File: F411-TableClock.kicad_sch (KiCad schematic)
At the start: 43 parts, among them J1 USB_C_Receptacle_USB2.0_16P, J2 Conn_01x16_Socket, J4 Conn_01x04_Pin, J5 Conn_01x08_Socket, J6 Conn_01x08_Pin, Q1 DMG3415U, Q2 BC547, SW1 SW_Push, SW2 SW_Push, SW3 SW_Push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

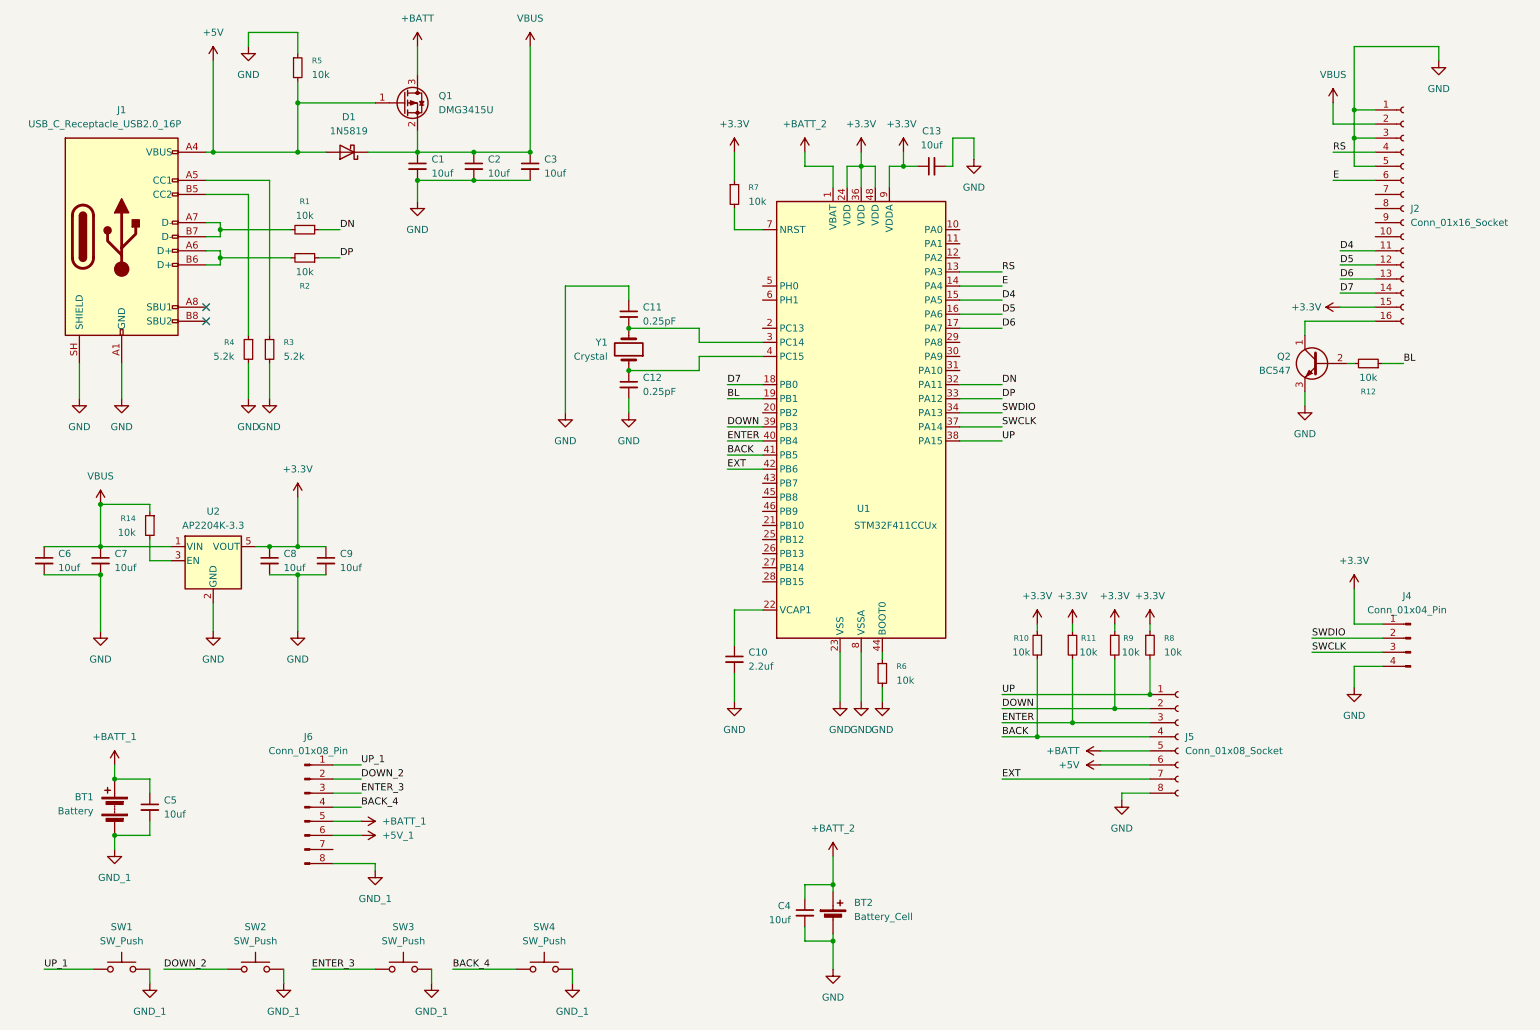
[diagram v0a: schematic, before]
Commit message: DHT added F411 table clock
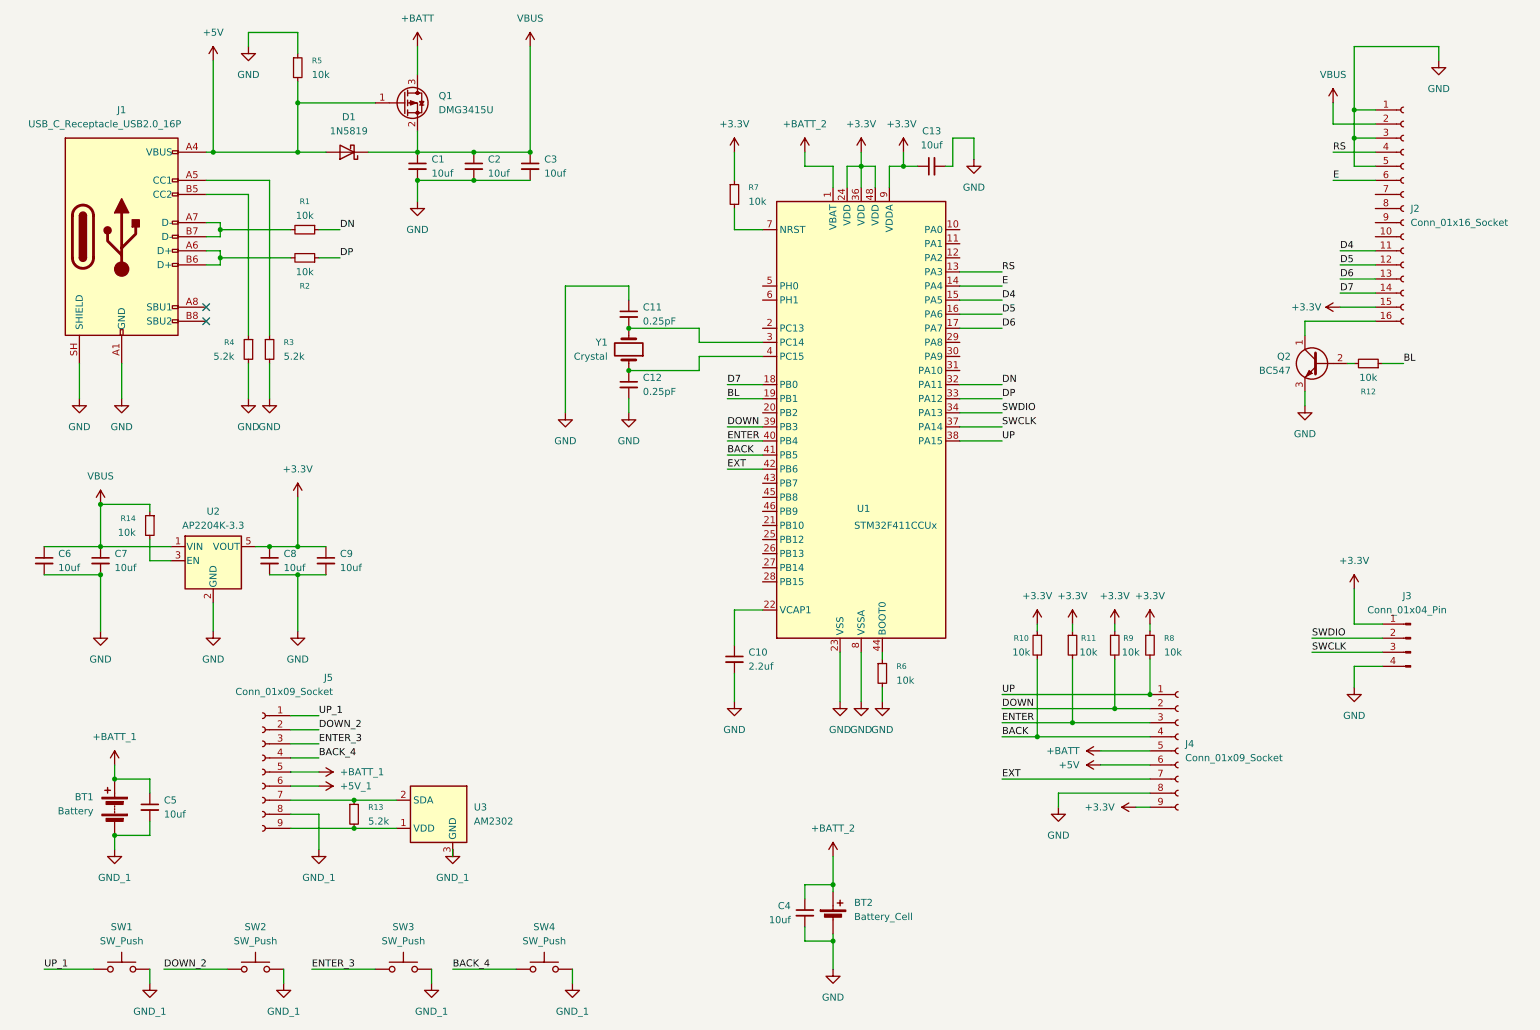
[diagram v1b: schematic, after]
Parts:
- removed J5: Conn_01x08_Socket, Connector_PinSocket_2.54mm:PinSocket_1x08_P2.54mm_Vertical, symbol Connector:Conn_01x08_Socket
- removed J6: Conn_01x08_Pin, Connector_PinHeader_2.54mm:PinHeader_1x08_P2.54mm_Vertical, symbol Connector:Conn_01x08_Pin
- added J4: Conn_01x09_Socket, Connector_PinSocket_2.54mm:PinSocket_1x09_P2.54mm_Vertical, symbol Connector:Conn_01x09_Socket
- added J5: Conn_01x09_Socket, Connector_PinHeader_2.54mm:PinHeader_1x09_P2.54mm_Vertical, symbol Connector:Conn_01x09_Socket
- added R13: 5.2k, Resistor_SMD:R_0805_2012Metric, symbol Device:R_Small
- added U3: AM2302, Sensor:ASAIR_AM2302_P2.54mm_Vertical, symbol Sensor:AM2302
- renumbered J4 to J3
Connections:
- net +3.3V: now also J4.9 (Pin_9)
- net +5V: now also J4.6 (Pin_6)
- net +5V_1: now also J5.6 (Pin_6)
- net +BATT: now also J4.5 (Pin_5)
- net +BATT_1: now also J5.5 (Pin_5)
- net BACK: now also J4.4 (Pin_4)
- net BACK_4: now also J5.4 (Pin_4)
- net DOWN: now also J4.2 (Pin_2)
- net DOWN_2: now also J5.2 (Pin_2)
- net ENTER: now also J4.3 (Pin_3)
- net ENTER_3: now also J5.3 (Pin_3)
- net EXT: now also J4.7 (Pin_7)
- net GND: now also J4.8 (Pin_8)
- net GND_1: now also J5.8 (Pin_8), U3.3 (GND), U3.4 (GND)
- net UP: now also J4.1 (Pin_1)
- net UP_1: now also J5.1 (Pin_1)
- new net: J5.9 (Pin_9), R13.2, U3.1 (VDD)
- new net: J5.7 (Pin_7), R13.1, U3.2 (SDA)
